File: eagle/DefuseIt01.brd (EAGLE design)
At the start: 100 x 69.2 mm, 32 parts, among them IC1 74HCT138N, IC2 74HCT138N, IC3 74HCT245N, J1 22-27-2061-06, J10 22-27-2061-06, J11 22-27-2061-06, J12 22-27-2061-06, J13 22-27-2061-06, J14 22-27-2061-06, J15 22-27-2061-06, J16 22-27-2061-06, J17 22-27-2021-02, J18 22-27-2031-03, J19 22-27-2031-03, J2 22-27-2061-06, J20 22-27-2021-02, J3 22-27-2061-06, J4 22-27-2061-06, J5 22-27-2061-06, J6 22-27-2061-06, J7 22-27-2061-06, J8 22-27-2061-06, J9 22-27-2061-06

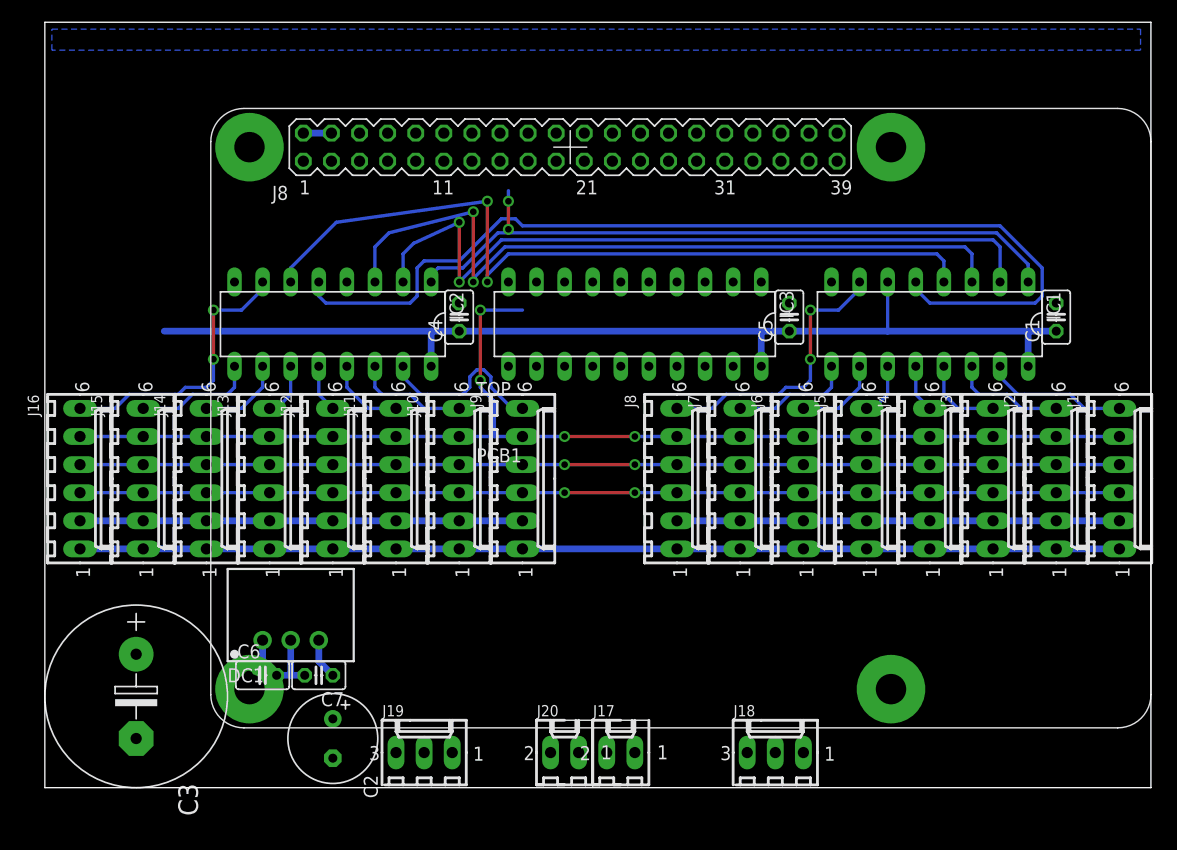
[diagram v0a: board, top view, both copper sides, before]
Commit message: Finished first layout w/o audio
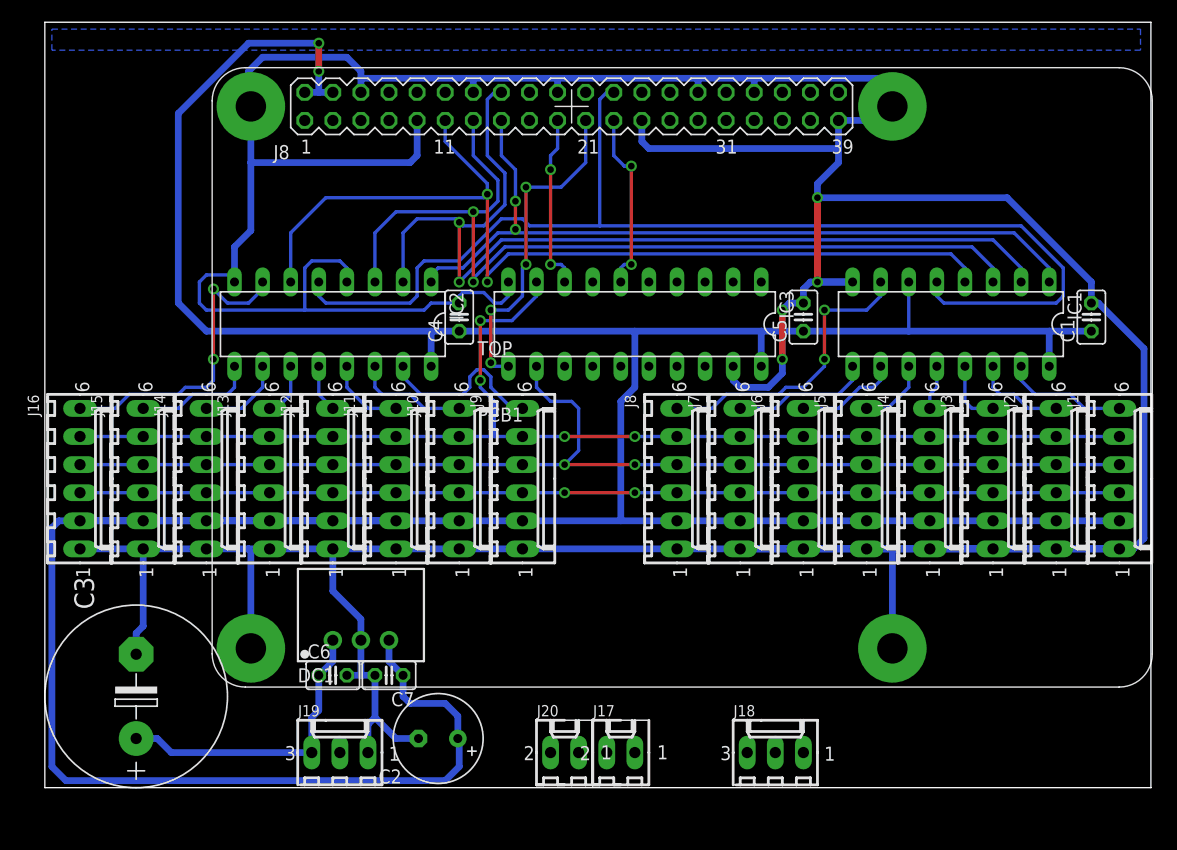
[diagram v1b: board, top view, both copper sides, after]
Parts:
- moved C2 9.53 mm to (35.6, 4.45), turned to 180 degrees
- moved J19 7.62 mm to (26.7, 3.17)
- moved C6 6.35 mm to (26.0, 10.2)
- moved C7 6.35 mm to (31.1, 10.2)
- moved DC1 6.35 mm to (28.6, 13.3)
- moved PCB1 3.69 mm to (15.1, 9.10)
- moved C1 3.17 mm to (94.6, 42.5)
- moved IC1 1.91 mm to (81.9, 41.9)
- moved C5 1.27 mm to (68.6, 42.5)
- turned C3 to 90 degrees
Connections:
- removed net I-SPI-CLK: PCB1.23
- new net I-SPI-SCK: IC3.6, PCB1.23
- new net SPI-SCK: IC3.14
- net +5V: now also IC3.1
- net GND: now also IC3.19
- net I-SPI-MISO: now also IC3.11
- net I-SPI-MOSI: now also IC3.8
- net SPI-MISO: now also IC3.9
- net SPI-MOSI: now also IC3.12
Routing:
- net GND: track 99.7 -> 457.0 mm, vias 0 -> 4
- net +5V: track 180.9 -> 355.3 mm, vias 0 -> 2
- net I-SPI-MISO: track 0.00 -> 30.0 mm, vias 0 -> 4
- net +12V: track 3.70 -> 27.4 mm
- net A1: track 67.7 -> 87.0 mm
- net I-SPI-SCK: track 0.00 -> 16.4 mm, vias 0 -> 2
- net I-SPI-MOSI: track 0.00 -> 16.0 mm, vias 0 -> 2
- net SPI-SS: track 88.8 -> 104.1 mm
- net A2: track 68.6 -> 81.9 mm
- net A3: track 73.1 -> 86.3 mm
- net SPI-MOSI: track 94.0 -> 106.1 mm
- net A0: track 62.8 -> 71.4 mm
- net SPI-MISO: track 109.7 -> 112.3 mm
- net N$16: track 25.3 -> 27.5 mm
- net N$4: track 10.3 -> 8.41 mm
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
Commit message: added audio chip; layout correction
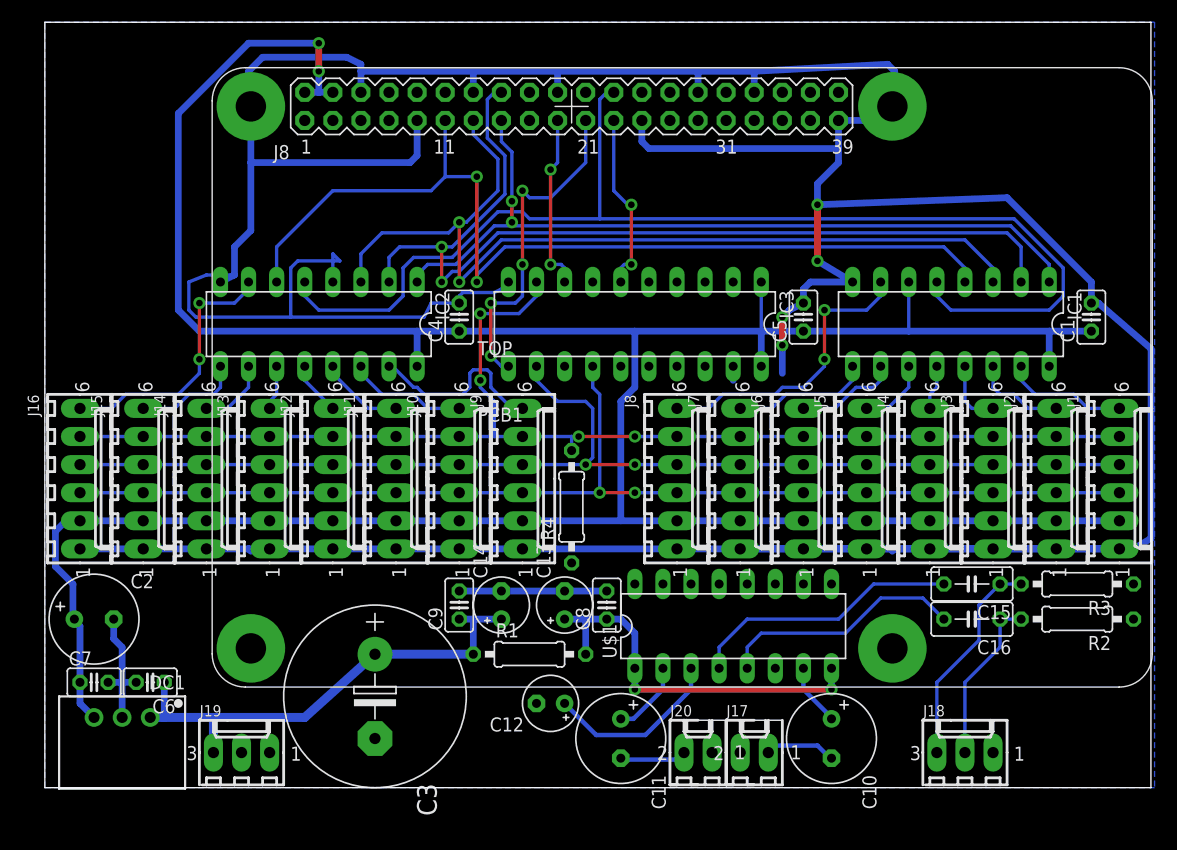
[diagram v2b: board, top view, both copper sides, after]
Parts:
- added C10, C11: (no value), rcl:E3,5-8
- added C12, C13, C14: (no value), rcl:E2,5-5
- added C15, C16: (no value), rcl:C050-030X075
- added C8, C9: 100n, rcl:C025-025X050
- added R1, R2, R3, R4: (no value), rcl:0207/10
- added U$1: TDA7268, JKD:DIL16
- moved C2 32.9 mm to (4.45, 15.2), turned to 0 degrees
- moved C7 26.7 mm to (4.45, 9.53), turned to 0 degrees
- moved DC1 22.7 mm to (6.99, 6.35), turned to 180 degrees
- moved C3 21.6 mm to (29.8, 8.26), turned to 270 degrees
- moved J18 17.1 mm to (83.2, 3.17)
- moved C6 16.5 mm to (9.53, 9.53), turned to 180 degrees
- moved J17 12.1 mm to (64.1, 3.17)
- moved J20 12.1 mm to (59.1, 3.17)
- moved J19 8.89 mm to (17.8, 3.17)
- moved IC2 1.27 mm to (24.8, 41.9)
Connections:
- removed net SPI-CLK: J1.3, J10.3, J11.3, J12.3, J13.3, J14.3, J15.3, J16.3, J2.3, J3.3, J4.3, J5.3, J6.3, J7.3, J8.3, J9.3
- new net N$17: C16.2, U$1.5
- new net N$18: C12.+, U$1.3
- new net N$19: C10.+, U$1.7
- new net N$20: C11.+, U$1.2
- new net N$21: C11.-, J20.2
- new net N$22: C10.-, J17.1
- new net N$23: C13.+, C8.1, R1.2, U$1.1, U$1.8
- new net N$25: C15.2, U$1.4
- new net N$26: C16.1, J18.2, R2.2
- new net N$27: C15.1, J18.3, R3.2
- net +12V: now also C14.+, C9.1, R1.1
- net GND: now also C12.-, C13.-, C14.-, C8.2, C9.2, J17.2, J18.1, J20.1, R2.1, R3.1, R4.1, U$1.10, U$1.11, U$1.12, U$1.13, U$1.14, U$1.15, U$1.16, U$1.6, U$1.9
- net SPI-MISO: now also R4.2
- net SPI-SCK: now also J1.3, J10.3, J11.3, J12.3, J13.3, J14.3, J15.3, J16.3, J2.3, J3.3, J4.3, J5.3, J6.3, J7.3, J8.3, J9.3
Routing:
- net SPI-SCK: track 0.00 -> 105.7 mm, vias 0 -> 2
- net SPI-CLK: track 94.0 -> 0.00 mm, vias 2 -> 0
- net +5V: track 355.3 -> 274.4 mm
- net N$23: track 0.00 -> 34.8 mm, vias 0 -> 2
- net GND: track 457.0 -> 431.4 mm
- net N$25: track 0.00 -> 24.6 mm
- net N$17: track 0.00 -> 22.3 mm
- net N$27: track 0.00 -> 19.5 mm
- net +12V: track 27.4 -> 44.7 mm
- net N$18: track 0.00 -> 16.2 mm
- net N$26: track 0.00 -> 15.3 mm
- net N$20: track 0.00 -> 6.82 mm
- net N$21: track 0.00 -> 6.66 mm
- net N$22: track 0.00 -> 6.45 mm
- net N$19: track 0.00 -> 5.62 mm
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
